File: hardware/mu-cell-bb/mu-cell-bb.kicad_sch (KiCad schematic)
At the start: 75 parts, among them IC1 SX1255IWLTRT, J1 TX, J2 RX, J3 EXT_CLK, J4 RPi GPIO, J5 IO, Q1 BC817-40W, Q2 BC817-40W, U1 24LC256, U2 LDK130M33R, Y1 32MHz

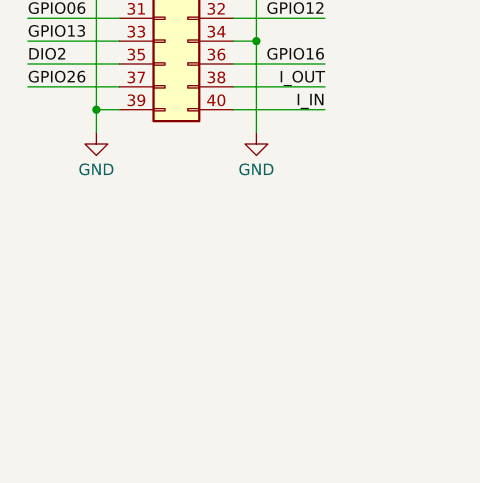
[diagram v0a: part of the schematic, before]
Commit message: linted readme, moved stuff on PCB
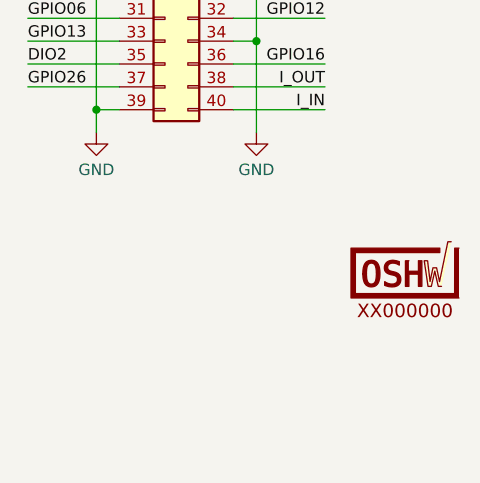
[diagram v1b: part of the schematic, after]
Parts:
- added LOGO1: ~, OSHW:OSHW-Certification-Mark-Stacked_8x7mm_SilkMask, symbol OSHW:OSHW_Certification_Mark_Stacked_Medium
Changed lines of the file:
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@@
+	)
+	(symbol
+		(lib_id "OSHW:OSHW_Certification_Mark_Stacked_Medium")
+		(at 274.32 172.72 0)
+		(unit 1)
+		(exclude_from_sim no)
+		(in_bom no)
+		(on_board yes)
+		(dnp no)
+		(fields_autoplaced yes)
+		(property "Reference" "LOGO1"
+			(at 274.32 172.72 0)
+			(effects
+				(font
+					(size 1.27 1.27)
+				)
+				(hide yes)
+			)
+		)
+		(property "Value" "~"
+			(at 274.32 172.72 0)
+			(effects
+				(font
+					(size 1.27 1.27)
+				)
+				(hide yes)
+			)
+		)
+		(property "Footprint" "OSHW:OSHW-Certification-Mark-Stacked_8x7mm_SilkMask"
+			(at 274.32 172.72 0)
+			(effects
+				(font
+					(size 1.27 1.27)
+				)
+				(hide yes)
+			)
+		)
+		(property "Datasheet" ""
+			(at 274.32 172.72 0)
+			(effects
+				(font
+					(size 1.27 1.27)
+				)
+				(hide yes)
+			)
+		)
+		(property "Description" "OSHW Certification Mark, Stacked"
+			(at 274.32 172.72 0)
+			(effects
+				(font
+					(size 1.27 1.27)
+				)
+				(hide yes)
+			)
+		)
+		(instances
+			(project ""
+				(path "/564c8f3e-4a0a-4bb3-921f-1318a09780f9"
+					(reference "LOGO1")
+					(unit 1)
+				)
+			)
+		)
 	)
 	(symbol

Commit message: saved changes on PCB
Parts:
- removed LOGO1: ~, OSHW:OSHW-Certification-Mark-Stacked_8x7mm_SilkMask, symbol OSHW:OSHW_Certification_Mark_Stacked_Medium
- added BE000000: ~, OSHW:OSHW-Certification-Mark-Stacked_8x7mm_SilkMask, symbol OSHW:OSHW_Certification_Mark_Stacked_Medium
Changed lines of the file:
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@@
-	)
-	(symbol
-		(lib_id "OSHW:OSHW_Certification_Mark_Stacked_Medium")
-		(at 274.32 172.72 0)
-		(unit 1)
-		(exclude_from_sim no)
-		(in_bom no)
-		(on_board yes)
-		(dnp no)
-		(fields_autoplaced yes)
-		(property "Reference" "LOGO1"
-			(at 274.32 172.72 0)
-			(effects
-				(font
-					(size 1.27 1.27)
-				)
-				(hide yes)
-			)
-		)
-		(property "Value" "~"
-			(at 274.32 172.72 0)
-			(effects
-				(font
-					(size 1.27 1.27)
-				)
-				(hide yes)
-			)
-		)
-		(property "Footprint" "OSHW:OSHW-Certification-Mark-Stacked_8x7mm_SilkMask"
-			(at 274.32 172.72 0)
-			(effects
-				(font
-					(size 1.27 1.27)
-				)
-				(hide yes)
-			)
-		)
-		(property "Datasheet" ""
-			(at 274.32 172.72 0)
-			(effects
-				(font
-					(size 1.27 1.27)
-				)
-				(hide yes)
-			)
-		)
-		(property "Description" "OSHW Certification Mark, Stacked"
-			(at 274.32 172.72 0)
-			(effects
-				(font
-					(size 1.27 1.27)
-				)
-				(hide yes)
-			)
-		)
-		(instances
-			(project ""
-				(path "/564c8f3e-4a0a-4bb3-921f-1318a09780f9"
-					(reference "LOGO1")
-					(unit 1)
-				)
-			)
-		)
 	)
 	(symbol
@@
 					(unit 1)
 				)
+			)
+		)
+	)
+	(symbol
+		(lib_id "OSHW:OSHW_Certification_Mark_Stacked_Medium")
+		(at 275.59 172.72 0)
+		(unit 1)
+		(exclude_from_sim no)
+		(in_bom no)
+		(on_board yes)
+		(dnp no)
+		(fields_autoplaced yes)
+		(property "Reference" "BE000000"
+			(at 275.59 177.292 0)
+			(do_not_autoplace yes)
+			(effects
+				(font
+					(size 1.5 1.5)
+				)
+			)
+		)
+		(property "Value" "~"
+			(at 275.59 172.72 0)
+			(effects
+				(font
+					(size 1.27 1.27)
+				)
+				(hide yes)
+			)
+		)
+		(property "Footprint" "OSHW:OSHW-Certification-Mark-Stacked_8x7mm_SilkMask"
+			(at 275.59 172.72 0)
+			(effects
+				(font
+					(size 1.27 1.27)
+				)
+				(hide yes)
+			)
+		)
+		(property "Datasheet" ""
+			(at 275.59 172.72 0)
+			(effects
+				(font
+					(size 1.27 1.27)
+				)
+				(hide yes)
+			)
+		)
+		(property "Description" "OSHW Certification Mark, Stacked"
+			(at 275.59 172.72 0)
+			(effects
+				(font
+					(size 1.27 1.27)
+				)
+				(hide yes)
+			)
+		)
+		(instances
+			(project ""
+				(path "/564c8f3e-4a0a-4bb3-921f-1318a09780f9"
+					(reference "BE000000")
+					(unit 1)
+				)

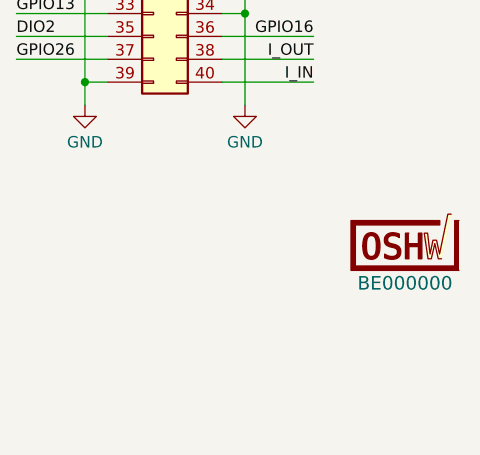
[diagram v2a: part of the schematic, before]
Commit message: updated silkscreens on PCB
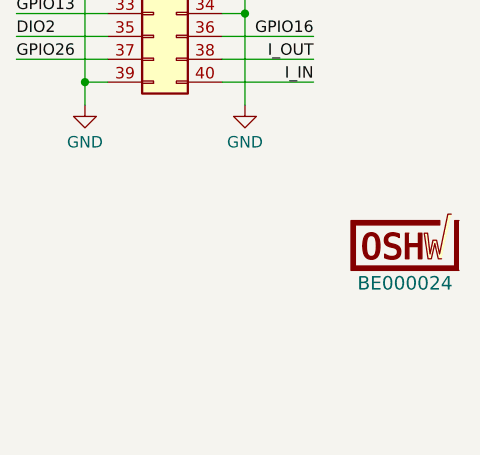
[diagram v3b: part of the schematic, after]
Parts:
- renumbered BE000000 to BE000024
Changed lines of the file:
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@@
 		(dnp no)
 		(fields_autoplaced yes)
-		(property "Reference" "BE000000"
+		(property "Reference" "BE000024"
 			(at 275.59 177.292 0)
 			(do_not_autoplace yes)
@@
 			(project ""
 				(path "/564c8f3e-4a0a-4bb3-921f-1318a09780f9"
-					(reference "BE000000")
+					(reference "BE000024")
 					(unit 1)
 				)

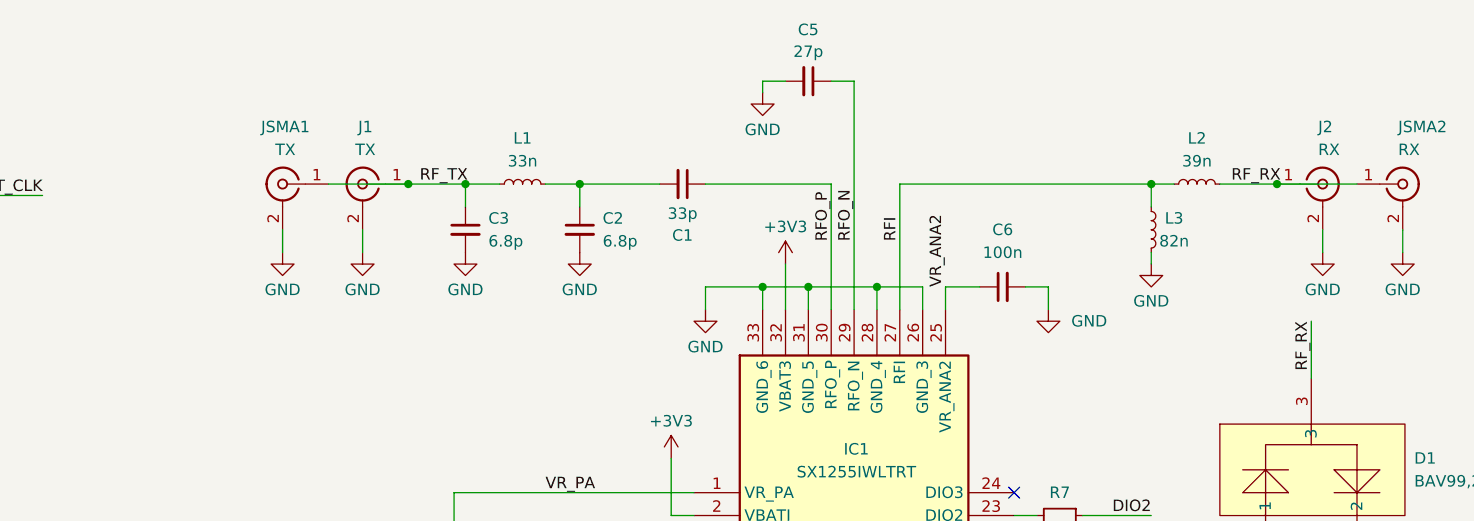
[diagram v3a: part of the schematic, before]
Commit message: updated RX an TX front end
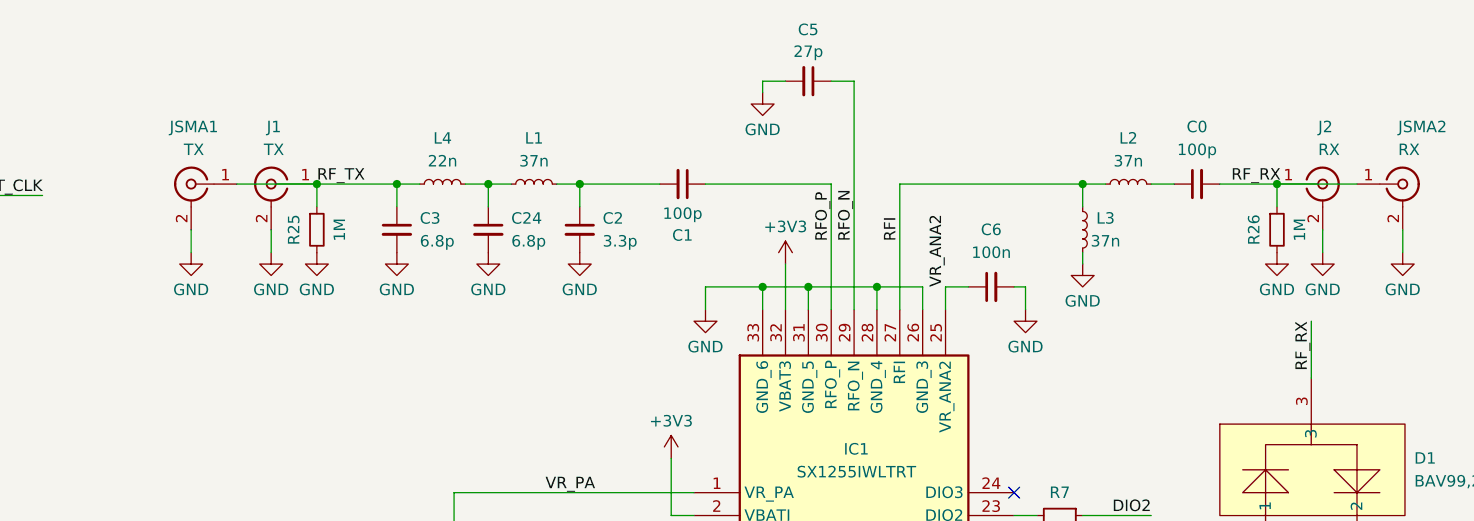
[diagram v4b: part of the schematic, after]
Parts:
- added C0: 100p, Capacitor_SMD:C_0402_1005Metric_Pad0.74x0.62mm_HandSolder, symbol Device:C_Small
- added C24: 6.8p, Capacitor_SMD:C_0402_1005Metric_Pad0.74x0.62mm_HandSolder, symbol Device:C_Small
- added L4: 22n, Inductor_SMD:L_0402_1005Metric_Pad0.77x0.64mm_HandSolder, symbol Device:L_Small
- added R25, R26: 1M, Resistor_SMD:R_0402_1005Metric_Pad0.72x0.64mm_HandSolder, symbol Device:R_Small
- C1: value 33p -> 100p; LCSC Part C437439 -> (none)
- C2: value 6.8p -> 3.3p; LCSC Part C1864373 -> (none)
- L1: value 33n -> 37n; LCSC Part C39885562 -> (none); MPN AISC-0603-R039J-T -> (none)
- L2: value 39n -> 37n; LCSC Part C40399699 -> (none); MPN AISC-0603-R039J-T -> (none)
- L3: value 82n -> 37n; LCSC Part C38907014 -> (none); MPN AISC-0603-R082J-T -> (none)
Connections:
- net GND: now also C24.2, R25.2, R26.2
- net RF_RX: now also C0.2, R26.1; no longer L2.1
- net RF_TX: now also L4.2, R25.1; no longer L1.2
- new net: C0.1, L2.1
- new net: C24.1, L1.2, L4.1
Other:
- moved on the sheet: C3, C6, J1, JSMA1, L1, L2, L3

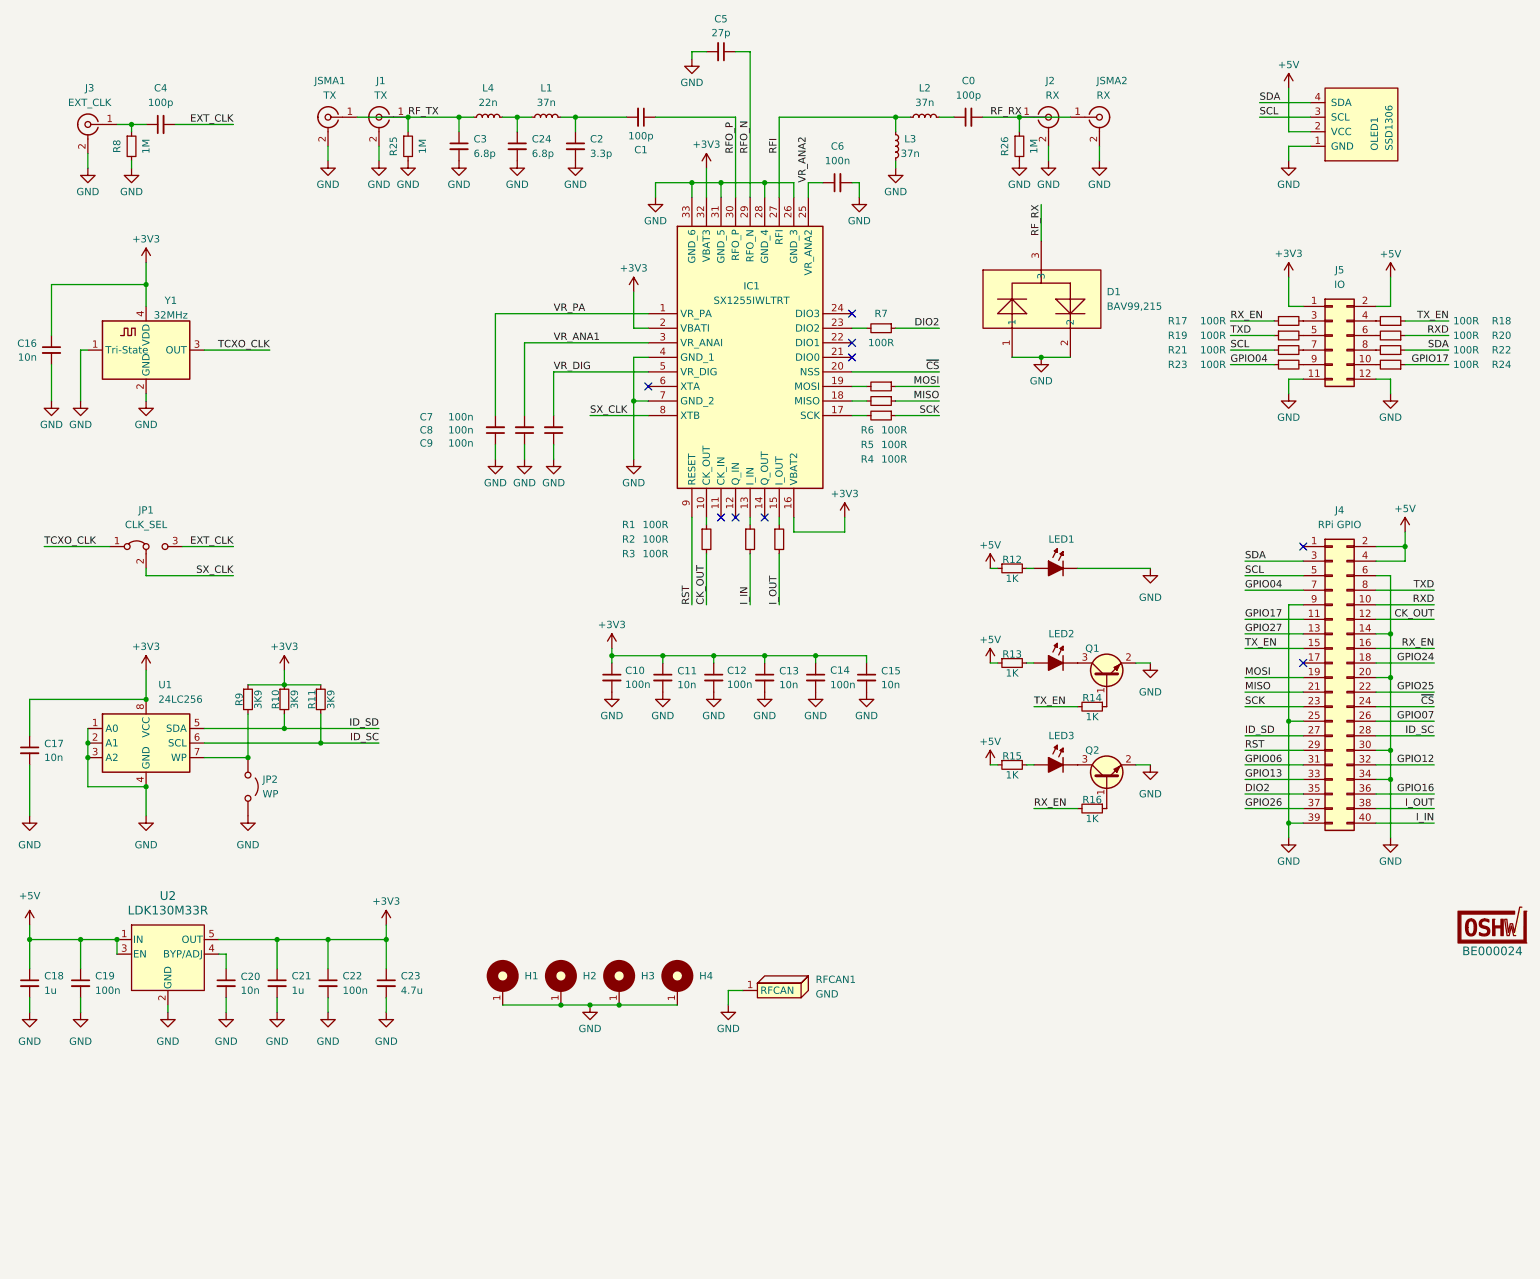
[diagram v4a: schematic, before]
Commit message: updated TX and RX front ends
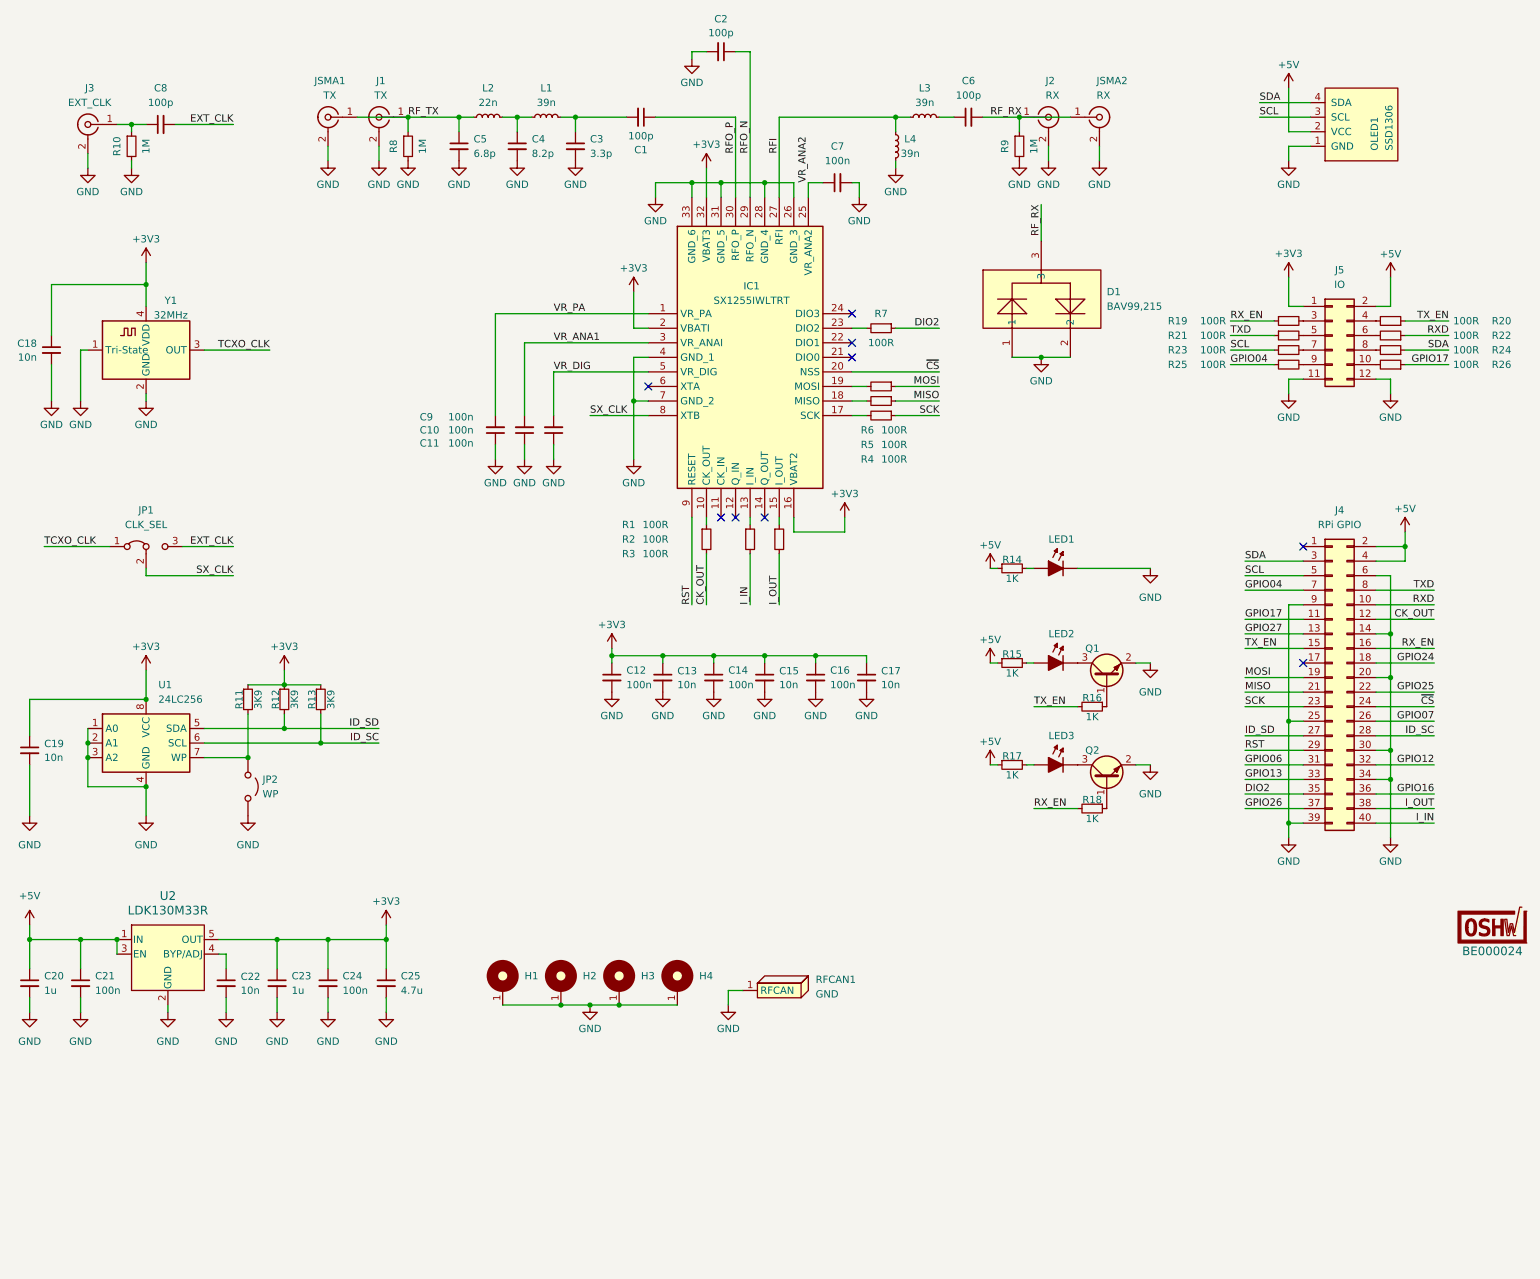
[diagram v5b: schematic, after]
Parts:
- removed R25, R26: 1M, Resistor_SMD:R_0402_1005Metric_Pad0.72x0.64mm_HandSolder, symbol Device:R_Small
- added R8, R9: 1M, Resistor_SMD:R_0402_1005Metric_Pad0.72x0.64mm_HandSolder, symbol Device:R_Small
- C2: renamed from C5; value 27p -> 100p; LCSC Part C3889037 -> (none); MPN AC0603JRNPO9BN270 -> (none)
- C4: renamed from C24; value 6.8p -> 8.2p
- L1: value 37n -> 39n
- L3: renamed from L2; value 37n -> 39n
- L4: renamed from L3; value 37n -> 39n
- renumbered C8 to C10, C9 to C11, C10 to C12, C11 to C13, C12 to C14, C13 to C15, C14 to C16, C15 to C17, C16 to C18, C17 to C19, C18 to C20, C19 to C21, C20 to C22, C21 to C23, C22 to C24, C23 to C25, C2 to C3, C3 to C5, C0 to C6, C6 to C7, C4 to C8, C7 to C9, L4 to L2, R8 to R10, R9 to R11, R10 to R12, R11 to R13, R12 to R14, R13 to R15, R14 to R16, R15 to R17, R16 to R18, R17 to R19, R18 to R20, R19 to R21, R20 to R22, R21 to R23, R22 to R24, R23 to R25, R24 to R26
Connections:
- net GND: now also R8.2, R9.2
- net RF_RX: now also R9.1
- net RF_TX: now also R8.1
